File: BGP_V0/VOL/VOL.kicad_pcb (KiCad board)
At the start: 2 copper layers, 34 x 30 mm, 23 parts, among them IC1 TC7660SO-08, P1 CONN_01X05, P2 CONN_01X03, P3 CONN_01X05, P4 CONN_01X05, P5 CONN_01X02

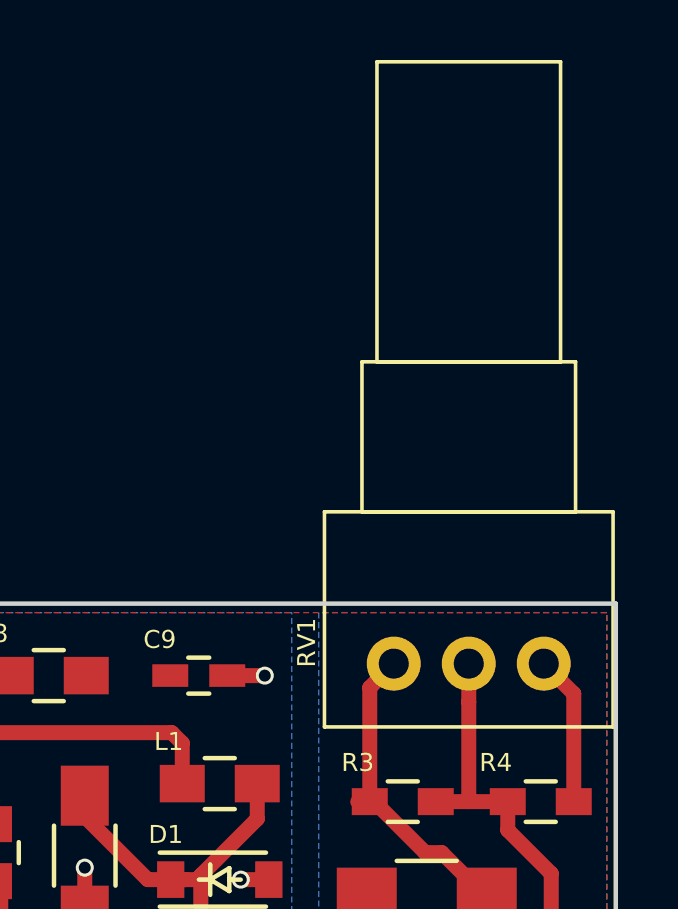
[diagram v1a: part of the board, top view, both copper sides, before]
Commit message: Pot fixups for silkscreen overlap
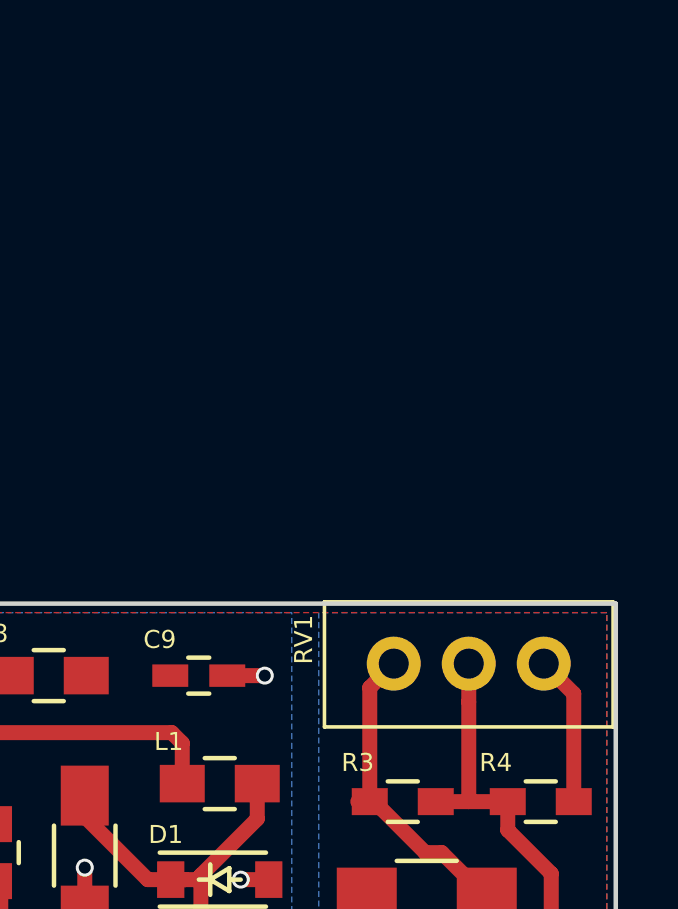
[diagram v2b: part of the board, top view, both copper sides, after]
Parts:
- RV1: footprint Potentiometers:Potentiometer_Alps_RK097_Single_Vertical -> LIBS:Potentiometer_Alps_RK097_Single_Vertical
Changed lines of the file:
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@@
-(kicad_pcb (version 4) (host pcbnew 4.0.7)
+(kicad_pcb (version 4) (host pcbnew 4.0.4-1.fc24-product)
   (general
     (links 45)
     (no_connects 0)
-    (area 151.305 31.424999 187.955 80.075001)
+    (area 151.305 49.474999 188.275 80.075001)
     (thickness 1.6)
     (drawings 31)
@@
     (add_net Earth)
   )
-  (module Potentiometers:Potentiometer_Alps_RK097_Single_Vertical (layer F.Cu)
-    (at 183.6 52 90)
-    (descr "Potentiometer, vertically mounted, Omeg PC16PU, Omeg PC16PU, Omeg PC16PU, Vishay/Spectrol 248GJ/249GJ Single, Vishay/Spectrol 248GJ/249GJ Single, Vishay/Spectrol 248GJ/249GJ Single, Vishay/Spectrol 248GH/249GH Single, Vishay/Spectrol 148/149 Single, Vishay/Spectrol 148/149 Single, Vishay/Spectrol 148/149 Single, Vishay/Spectrol 148A/149A Single with mounting plates, Vishay/Spectrol 148/149 Double, Vishay/Spectrol 148A/149A Double with mounting plates, Piher PC-16 Single, Piher PC-16 Single, Piher PC-16 Single, Piher PC-16SV Single, Piher PC-16 Double, Piher PC-16 Triple, Piher T16H Single, Piher T16L Single, Piher T16H Double, Alps RK163 Single, Alps RK163 Double, Alps RK097 Single, http://www.alps.com/prod/info/E/HTML/Potentiometer/RotaryPotentiometers/RK097/RK097111080J.html")
-    (tags "Potentiometer vertical  Omeg PC16PU  Omeg PC16PU  Omeg PC16PU  Vishay/Spectrol 248GJ/249GJ Single  Vishay/Spectrol 248GJ/249GJ Single  Vishay/Spectrol 248GJ/249GJ Single  Vishay/Spectrol 248GH/249GH Single  Vishay/Spectrol 148/149 Single  Vishay/Spectrol 148/149 Single  Vishay/Spectrol 148/149 Single  Vishay/Spectrol 148A/149A Single with mounting plates  Vishay/Spectrol 148/149 Double  Vishay/Spectrol 148A/149A Double with mounting plates  Piher PC-16 Single  Piher PC-16 Single  Piher PC-16 Single  Piher PC-16SV Single  Piher PC-16 Double  Piher PC-16 Triple  Piher T16H Single  Piher T16L Single  Piher T16H Double  Alps RK163 Single  Alps RK163 Double  Alps RK097 Single")
-    (fp_text reference RV1 (at 0.7 -7.9 90) (layer F.SilkS)
-      (effects (font (size 0.6 0.6) (thickness 0.15)))
-    )
-    (fp_text value POT (at 0 3.5 90) (layer F.Fab) hide
-      (effects (font (size 0.6 0.6) (thickness 0.15)))
-    )
-    (fp_line (start -2.05 -7.25) (end -2.05 2.25) (layer F.Fab) (width 0.1))
-    (fp_line (start -2.05 2.25) (end 5 2.25) (layer F.Fab) (width 0.1))
-    (fp_line (start 5 2.25) (end 5 -7.25) (layer F.Fab) (width 0.1))
-    (fp_line (start 5 -7.25) (end -2.05 -7.25) (layer F.Fab) (width 0.1))
-    (fp_line (start 5 -6) (end 5 1) (layer F.Fab) (width 0.1))
-    (fp_line (start 5 1) (end 10 1) (layer F.Fab) (width 0.1))
-    (fp_line (start 10 1) (end 10 -6) (layer F.Fab) (width 0.1))
-    (fp_line (start 10 -6) (end 5 -6) (layer F.Fab) (width 0.1))
-    (fp_line (start 10 -5.5) (end 10 0.5) (layer F.Fab) (width 0.1))
-    (fp_line (start 10 0.5) (end 20 0.5) (layer F.Fab) (width 0.1))
-    (fp_line (start 20 0.5) (end 20 -5.5) (layer F.Fab) (width 0.1))
-    (fp_line (start 20 -5.5) (end 10 -5.5) (layer F.Fab) (width 0.1))
-    (fp_line (start -2.11 -7.31) (end 5.06 -7.31) (layer F.SilkS) (width 0.12))
-    (fp_line (start -2.11 2.31) (end 5.06 2.31) (layer F.SilkS) (width 0.12))
-    (fp_line (start -2.11 -7.31) (end -2.11 2.31) (layer F.SilkS) (width 0.12))
-    (fp_line (start 5.06 -7.31) (end 5.06 2.31) (layer F.SilkS) (width 0.12))
-    (fp_line (start 5.06 -6.06) (end 10.06 -6.06) (layer F.SilkS) (width 0.12))
-    (fp_line (start 5.06 1.06) (end 10.06 1.06) (layer F.SilkS) (width 0.12))
-    (fp_line (start 5.06 -6.06) (end 5.06 1.06) (layer F.SilkS) (width 0.12))
-    (fp_line (start 10.06 -6.06) (end 10.06 1.06) (layer F.SilkS) (width 0.12))
-    (fp_line (start 10.06 -5.56) (end 20.061 -5.56) (layer F.SilkS) (width 0.12))
-    (fp_line (start 10.06 0.56) (end 20.061 0.56) (layer F.SilkS) (width 0.12))
-    (fp_line (start 10.06 -5.56) (end 10.06 0.56) (layer F.SilkS) (width 0.12))
-    (fp_line (start 20.061 -5.56) (end 20.061 0.56) (layer F.SilkS) (width 0.12))
-    (fp_line (start -2.3 -7.5) (end -2.3 2.5) (layer F.CrtYd) (width 0.05))
-    (fp_line (start -2.3 2.5) (end 20.25 2.5) (layer F.CrtYd) (width 0.05))
-    (fp_line (start 20.25 2.5) (end 20.25 -7.5) (layer F.CrtYd) (width 0.05))
-    (fp_line (start 20.25 -7.5) (end -2.3 -7.5) (layer F.CrtYd) (width 0.05))
-    (pad 3 thru_hole circle (at 0 -5 90) (size 1.8 1.8) (drill 1) (layers *.Cu *.Mask)
-      (net 15 "Net-(C1-Pad1)"))
-    (pad 2 thru_hole circle (at 0 -2.5 90) (size 1.8 1.8) (drill 1) (layers *.Cu *.Mask)
-      (net 6 /JHOT))
-    (pad 1 thru_hole circle (at 0 0 90) (size 1.8 1.8) (drill 1) (layers *.Cu *.Mask)
-      (net 3 Earth))
-    (model Potentiometers.3dshapes/Potentiometer_Alps_RK097_Single_Vertical.wrl
-      (at (xyz 0 0 0))
-      (scale (xyz 0.393701 0.393701 0.393701))
-      (rotate (xyz 0 0 0))
-    )
-  )
   (module Capacitors_SMD:C_1206_HandSoldering (layer F.Cu)
     (at 179.7 59.6 180)
@@
       (rotate (xyz 0 0 0))
     )
+  )
+  (module LIBS:Potentiometer_Alps_RK097_Single_Vertical (layer F.Cu)
+    (at 183.6 52 90)
+    (descr "Potentiometer, vertically mounted, Omeg PC16PU, Omeg PC16PU, Omeg PC16PU, Vishay/Spectrol 248GJ/249GJ Single, Vishay/Spectrol 248GJ/249GJ Single, Vishay/Spectrol 248GJ/249GJ Single, Vishay/Spectrol 248GH/249GH Single, Vishay/Spectrol 148/149 Single, Vishay/Spectrol 148/149 Single, Vishay/Spectrol 148/149 Single, Vishay/Spectrol 148A/149A Single with mounting plates, Vishay/Spectrol 148/149 Double, Vishay/Spectrol 148A/149A Double with mounting plates, Piher PC-16 Single, Piher PC-16 Single, Piher PC-16 Single, Piher PC-16SV Single, Piher PC-16 Double, Piher PC-16 Triple, Piher T16H Single, Piher T16L Single, Piher T16H Double, Alps RK163 Single, Alps RK163 Double, Alps RK097 Single, http://www.alps.com/prod/info/E/HTML/Potentiometer/RotaryPotentiometers/RK097/RK097111080J.html")
+    (tags "Potentiometer vertical  Omeg PC16PU  Omeg PC16PU  Omeg PC16PU  Vishay/Spectrol 248GJ/249GJ Single  Vishay/Spectrol 248GJ/249GJ Single  Vishay/Spectrol 248GJ/249GJ Single  Vishay/Spectrol 248GH/249GH Single  Vishay/Spectrol 148/149 Single  Vishay/Spectrol 148/149 Single  Vishay/Spectrol 148/149 Single  Vishay/Spectrol 148A/149A Single with mounting plates  Vishay/Spectrol 148/149 Double  Vishay/Spectrol 148A/149A Double with mounting plates  Piher PC-16 Single  Piher PC-16 Single  Piher PC-16 Single  Piher PC-16SV Single  Piher PC-16 Double  Piher PC-16 Triple  Piher T16H Single  Piher T16L Single  Piher T16H Double  Alps RK163 Single  Alps RK163 Double  Alps RK097 Single")
+    (fp_text reference RV1 (at 0.8 -8 90) (layer F.SilkS)
+      (effects (font (size 0.6 0.6) (thickness 0.15)))
+    )
+    (fp_text value POT (at 0 3.5 90) (layer F.Fab) hide
+      (effects (font (size 0.6 0.6) (thickness 0.15)))
+    )
+    (fp_line (start -2.05 -7.25) (end -2.05 2.25) (layer F.Fab) (width 0.1))
+    (fp_line (start -2.05 2.25) (end 2 2.25) (layer F.Fab) (width 0.1))
+    (fp_line (start 2 2.25) (end 2 -7.25) (layer F.Fab) (width 0.1))
+    (fp_line (start 2 -7.25) (end -2.05 -7.25) (layer F.Fab) (width 0.1))
+    (fp_line (start -2.11 -7.31) (end 2.06 -7.31) (layer F.SilkS) (width 0.12))
+    (fp_line (start -2.11 2.31) (end 2.06 2.31) (layer F.SilkS) (width 0.12))
+    (fp_line (start -2.11 -7.31) (end -2.11 2.31) (layer F.SilkS) (width 0.12))
+    (fp_line (start 2.06 -7.31) (end 2.06 2.31) (layer F.SilkS) (width 0.12))
+    (fp_line (start -2.3 -7.5) (end -2.3 2.5) (layer F.CrtYd) (width 0.05))
+    (fp_line (start -2.3 2.5) (end 2.25 2.5) (layer F.CrtYd) (width 0.05))
+    (fp_line (start 2.25 2.5) (end 2.25 -7.5) (layer F.CrtYd) (width 0.05))
+    (fp_line (start 2.25 -7.5) (end -2.3 -7.5) (layer F.CrtYd) (width 0.05))
+    (pad 3 thru_hole circle (at 0 -5 90) (size 1.8 1.8) (drill 1) (layers *.Cu *.Mask)
+      (net 15 "Net-(C1-Pad1)"))
+    (pad 2 thru_hole circle (at 0 -2.5 90) (size 1.8 1.8) (drill 1) (layers *.Cu *.Mask)
+      (net 6 /JHOT))
+    (pad 1 thru_hole circle (at 0 0 90) (size 1.8 1.8) (drill 1) (layers *.Cu *.Mask)
+      (net 3 Earth))
+    (model Potentiometers.3dshapes/Potentiometer_Alps_RK097_Single_Vertical.wrl
+      (at (xyz 0 0 0))
+      (scale (xyz 0.393701 0.393701 0.393701))
+      (rotate (xyz 0 0 0))
+    )

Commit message: Concentric pot fixups for 0_BT Stack and 1_HPF
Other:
- board text added: "BGP V0.0 Volume"
- board text removed: "BGP V1.0 Volume"
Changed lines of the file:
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@@
     (links 45)
     (no_connects 0)
-    (area 151.305 49.474999 188.275 80.075001)
+    (area 151.305 49.424999 187.955 80.075001)
     (thickness 1.6)
     (drawings 31)
@@
     (effects (font (size 0.6 0.6) (thickness 0.15)) (justify mirror))
   )
-  (gr_text "BGP V1.0\nVolume" (at 155 51.8) (layer B.SilkS)
+  (gr_text "BGP V0.0\nVolume" (at 156 52) (layer B.SilkS)
     (effects (font (size 0.6 0.6) (thickness 0.15)) (justify mirror))
   )

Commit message: V_0 Updates for caps, gerbers updated
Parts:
- C1: footprint Capacitors_SMD:C_1206_HandSoldering -> Capacitors_Tantalum_SMD:TantalC_SizeR_EIA-2012
- C2, C4: footprint Capacitors_SMD:C_0603_HandSoldering -> Capacitors_SMD:C_0805_HandSoldering
- C5: footprint Capacitors_SMD:C_1206_HandSoldering -> Capacitors_SMD:C_0805_HandSoldering
- moved C5 1.03 mm to (168.6, 57.4), turned to 90 degrees
- moved C4 0.93 mm to (165.8, 57.4)
- moved C2 0.70 mm to (154.1, 58.9)
- moved C1 0.60 mm to (180.3, 59.6), turned to 0 degrees
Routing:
- net Net-(C4-Pad2): track 6.18 -> 7.92 mm
- net /BAT+: track 25.9 -> 24.3 mm
- net Net-(C3-Pad2): track 18.7 -> 19.4 mm

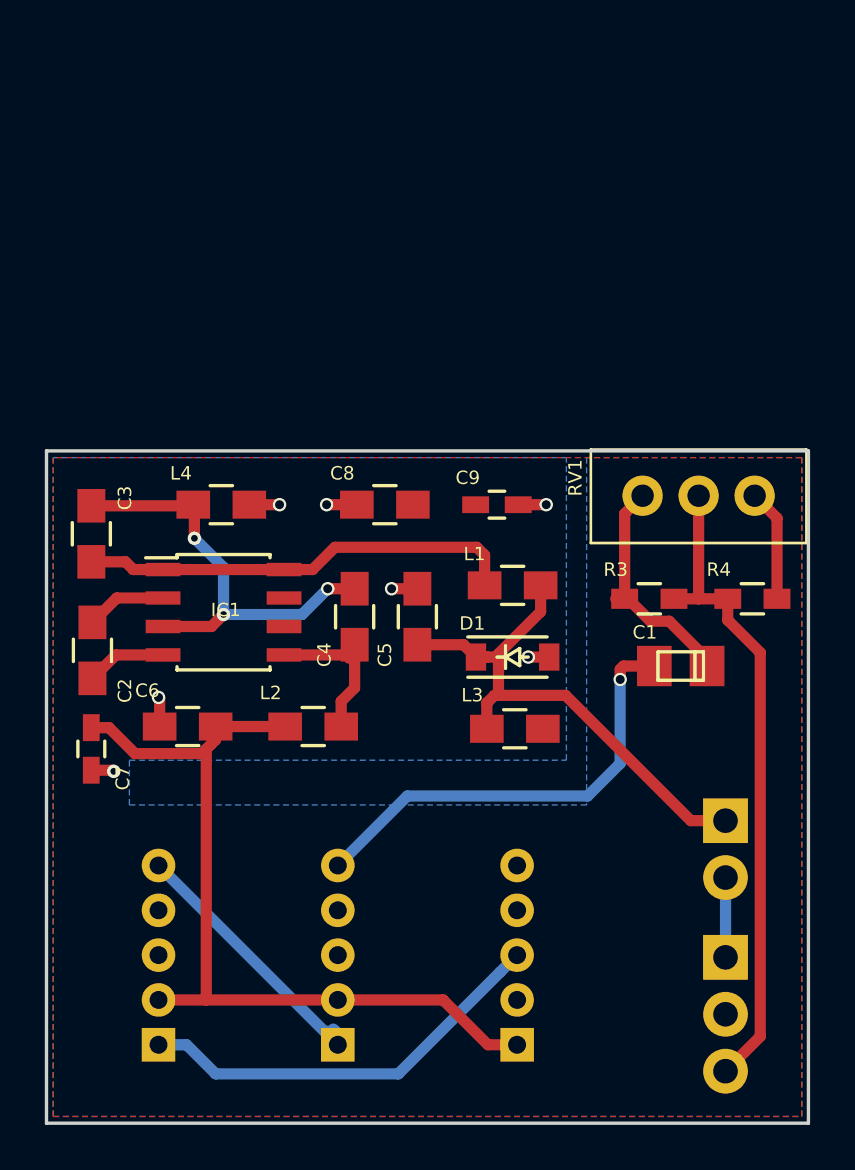
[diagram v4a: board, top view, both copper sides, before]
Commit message: Slight changes to Port layer placement - gerbers done
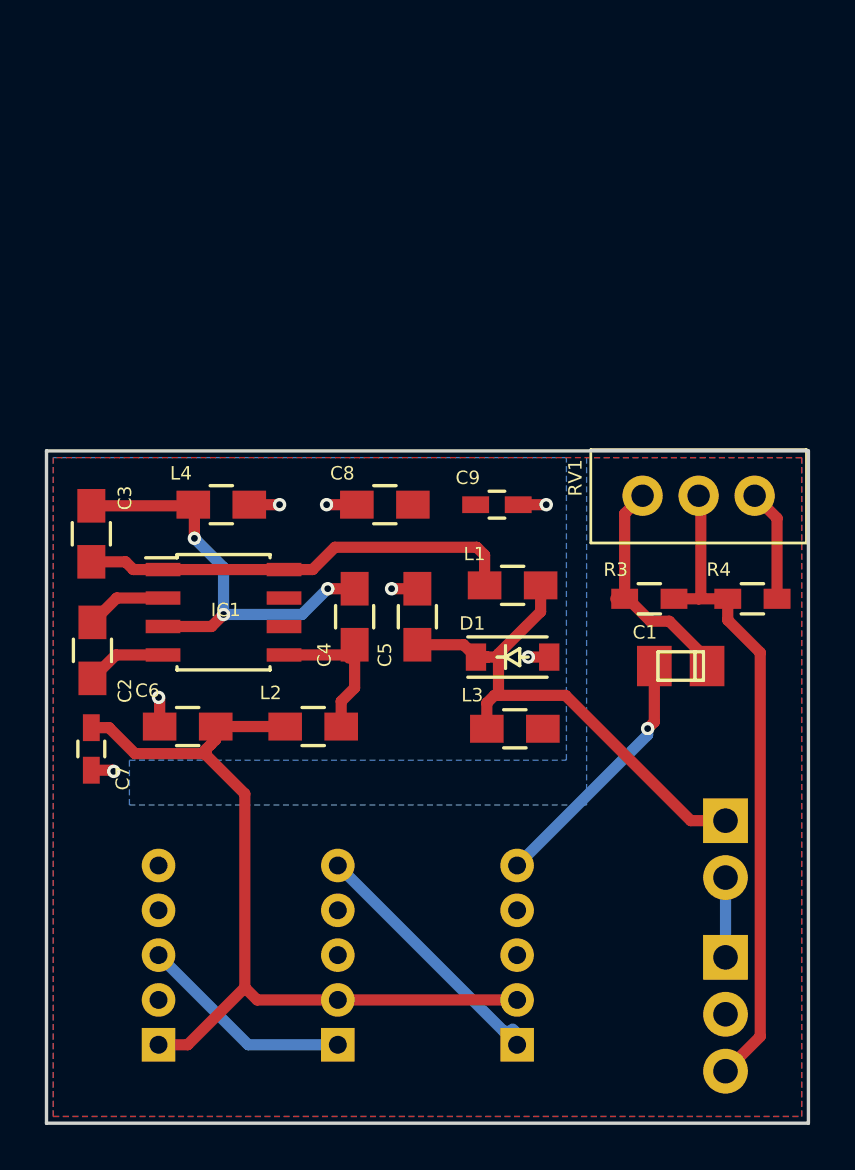
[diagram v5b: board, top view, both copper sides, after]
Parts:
- moved P1 16.0 mm to (157.0, 76.5)
- moved P3 8.00 mm to (165.0, 76.5)
- moved P4 8.00 mm to (173.0, 76.5)
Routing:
- net /BT_I: track 18.7 -> 9.66 mm
- net /M_O: track 20.3 -> 11.4 mm
- net /V-: track 38.0 -> 38.6 mm
